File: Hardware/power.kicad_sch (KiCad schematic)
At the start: 52 parts, among them J1 USB4110GFA, Q1 AO3407A, U1 TPS54302, U2 USBLC6-2SC6, U3 INA226, U4 AP63205WU, U5 AP2112K-3.3, U6 AP7343-33W5-7

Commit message: changed hella stuff in firmware plan and hardware pcb layout
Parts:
- removed D2, D3: PMEG3020EH, Diode_SMD:D_SOD-123F, symbol Diode:PMEG3020EH
- removed R6, R7: 0, Resistor_SMD:R_0402_1005Metric, symbol Device:R_Small
- removed R8, R9: 10k, Resistor_SMD:R_0402_1005Metric, symbol Device:R_Small
- C11, C12, C13, R10, R11, R12, U3: now not fitted; now left out of the parts list
- D5: footprint LED_SMD:LED_0402_1005Metric -> LED_SMD:LED_0805_2012Metric
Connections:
- net +5V_REG is gone; now on net +5V: C15.2, C16.2, L2.2, U4.1 (FB)
- net VBAT_Filtered: now also C1.1, C10.2, C2.1, U1.3 (VIN), U4.2 (EN), U4.3 (IN); no longer U3.8 (Vbus)
- net VBAT_MEASURE: no longer C1.1, C10.2, C2.1, U1.3 (VIN), U4.2 (EN), U4.3 (IN)
- net A0: no longer names the net of U3.2 (A0)
- net A1: no longer names the net of U3.1 (A1)
- net I2C2_SCL: no longer names the net of U3.5 (SCL)
- net I2C2_SDA: no longer names the net of U3.4 (SDA)
- net IN+: no longer names the net of C11.1, R10.1, U3.10 (Vin+)
- net IN-: no longer names the net of C11.2, R11.1, U3.9 (Vin-)
- net INA226_ALERT: no longer names the net of U3.3 (~{Alert})
- no-connect marks 4 -> 10

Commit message: hella shit configured, layout progress
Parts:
- C8: footprint Capacitor_SMD:C_0603_1608Metric -> Capacitor_SMD:C_0402_1005Metric
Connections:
- net +5V_USB is gone; now on net +5V: C9.1, J1.A4/B9 (VBUS), J1.B4/A9 (VBUS), U2.5 (VBUS)
- net VBAT renamed +VBAT

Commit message: added zener diode, more layout, Power verificatoin
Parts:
- added D2: BZT52C12-13-F, memo:(zener)SOD-123F_L2.8-W1.8-LS3.7-RD, symbol zener:BZT52C12-13-F
- C18, C20: value 0.1uF -> 1uF
- R3: value 0 -> 100k
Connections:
- net VBAT_Filtered: now also D2.1 (K)
- net at Q1.1 (G), R3.2: now also D2.2 (A)
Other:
- moved on the sheet: R3
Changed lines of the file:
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@@
 	)
 	(junction
-		(at 63.5 76.2)
+		(at 63.5 82.55)
 		(diameter 0)
 		(color 0 0 0 0)
@@
 	)
 	(junction
+		(at 63.5 73.66)
+		(diameter 0)
+		(color 0 0 0 0)
+	)
+	(junction
 		(at 128.27 208.28)
 		(diameter 0)
@@
 	)
 	(junction
-		(at 255.27 55.88)
+		(at 87.63 82.55)
 		(diameter 0)
 		(color 0 0 0 0)
 	)
 	(junction
-		(at 73.66 143.51)
+		(at 255.27 55.88)
 		(diameter 0)
 		(color 0 0 0 0)
 	)
 	(junction
-		(at 87.63 76.2)
+		(at 73.66 143.51)
 		(diameter 0)
 		(color 0 0 0 0)
@@
 	)
 	(junction
+		(at 72.39 59.69)
+		(diameter 0)
+		(color 0 0 0 0)
+	)
+	(junction
 		(at 276.86 222.25)
 		(diameter 0)
@@
 	(wire
 		(pts
+			(xy 87.63 83.82) (xy 87.63 82.55)
+		)
+		(stroke
+			(width 0)
+			(type default)
+		)
+	)
+	(wire
+		(pts
 			(xy 114.3 207.01) (xy 114.3 209.55)
 		)
@@
 	(wire
 		(pts
-			(xy 63.5 67.31) (xy 63.5 68.58)
+			(xy 63.5 67.31) (xy 63.5 73.66)
 		)
 		(stroke
@@
 	(wire
 		(pts
+			(xy 72.39 73.66) (xy 63.5 73.66)
+		)
+		(stroke
+			(width 0)
+			(type default)
+		)
+	)
+	(wire
+		(pts
 			(xy 351.79 90.17) (xy 370.84 90.17)
 		)
@@
 	(wire
 		(pts
-			(xy 68.58 59.69) (xy 80.01 59.69)
+			(xy 68.58 59.69) (xy 72.39 59.69)
 		)
 		(stroke
@@
 	(wire
 		(pts
+			(xy 87.63 71.12) (xy 87.63 77.47)
+		)
+		(stroke
+			(width 0)
+			(type default)
+		)
+	)
+	(wire
+		(pts
 			(xy 232.41 248.92) (xy 232.41 252.73)
 		)
@@
 	(wire
 		(pts
-			(xy 43.18 71.12) (xy 43.18 76.2)
+			(xy 43.18 71.12) (xy 43.18 82.55)
 		)
 		(stroke
@@
 	(wire
 		(pts
+			(xy 72.39 62.23) (xy 72.39 59.69)
+		)
+		(stroke
+			(width 0)
+			(type default)
+		)
+	)
+	(wire
+		(pts
 			(xy 248.92 252.73) (xy 250.19 252.73)
 		)
@@
 	(wire
 		(pts
+			(xy 87.63 77.47) (xy 87.63 82.55)
+		)
+		(stroke
+			(width 0)
+			(type default)
+		)
+	)
+	(wire
+		(pts
 			(xy 246.38 86.36) (xy 246.38 88.9)
 		)
@@
 	(wire
 		(pts
-			(xy 87.63 76.2) (xy 87.63 77.47)
-		)
-		(stroke
-			(width 0)
-			(type default)
-		)
-	)
-	(wire
-		(pts
 			(xy 256.54 88.9) (xy 256.54 86.36)
 		)
@@
 	(wire
 		(pts
-			(xy 63.5 76.2) (xy 87.63 76.2)
+			(xy 63.5 82.55) (xy 87.63 82.55)
 		)
 		(stroke
@@
 	(wire
 		(pts
-			(xy 43.18 76.2) (xy 63.5 76.2)
+			(xy 43.18 82.55) (xy 63.5 82.55)
 		)
 		(stroke
@@
 	(wire
 		(pts
-			(xy 87.63 76.2) (xy 87.63 71.12)
-		)
-		(stroke
-			(width 0)
-			(type default)
-		)
-	)
-	(wire
-		(pts
 			(xy 40.64 119.38) (xy 31.75 119.38)
 		)
@@
 	(wire
 		(pts
-			(xy 87.63 77.47) (xy 87.63 78.74)
-		)
-		(stroke
-			(width 0)
-			(type default)
-		)
-	)
-	(wire
-		(pts
 			(xy 119.38 119.38) (xy 119.38 114.3)
 		)
@@
 	(wire
 		(pts
+			(xy 72.39 73.66) (xy 72.39 72.39)
+		)
+		(stroke
+			(width 0)
+			(type default)
+		)
+	)
+	(wire
+		(pts
 			(xy 243.84 58.42) (xy 240.03 58.42)
 		)
@@
 	(wire
 		(pts
-			(xy 63.5 73.66) (xy 63.5 76.2)
+			(xy 63.5 80.01) (xy 63.5 82.55)
 		)
 		(stroke
@@
 	(wire
 		(pts
+			(xy 63.5 73.66) (xy 63.5 74.93)
+		)
+		(stroke
+			(width 0)
+			(type default)
+		)
+	)
+	(wire
+		(pts
 			(xy 391.16 214.63) (xy 403.86 214.63)
 		)
@@
 	(wire
 		(pts
+			(xy 72.39 59.69) (xy 80.01 59.69)
+		)
+		(stroke
+			(width 0)
+			(type default)
+		)
+	)
+	(wire
+		(pts
 			(xy 114.3 201.93) (xy 114.3 199.39)
 		)
@@
 	)
 	(symbol
+		(lib_id "zener:BZT52C12-13-F")
+		(at 72.39 67.31 270)
+		(unit 1)
+		(exclude_from_sim no)
+		(in_bom yes)
+		(on_board yes)
+		(dnp no)
+		(property "Reference" "D2"
+			(at 68.58 72.136 90)
+			(effects
+				(font
+					(size 0.762 0.762)
+					(thickness 0.0953)
+				)
+				(justify left)
+			)
+		)
+		(property "Value" "BZT52C12-13-F"
+			(at 68.58 74.676 90)
+			(effects
+				(font
+					(size 0.762 0.762)
+					(thickness 0.0953)
+				)
+				(justify left)
+			)
+		)
+		(property "Footprint" "memo:(zener)SOD-123F_L2.8-W1.8-LS3.7-RD"
+			(at 64.77 67.31 0)
+			(effects
+				(font
+					(size 1.27 1.27)
+				)
+				(hide yes)
+			)
+		)
+		(property "Datasheet" "https://lcsc.com/product-detail/Others_Diodes-Incorporated_BZT52C12-13-F_Diodes-Incorporated-BZT52C12-13-F_C177013.html"
+			(at 62.23 67.31 0)
+			(effects
+				(font
+					(size 1.27 1.27)
+				)
+				(hide yes)
+			)
+		)
+		(property "Description" ""
+			(at 72.39 67.31 0)
+			(effects
+				(font
+					(size 1.27 1.27)
+				)
+				(hide yes)
+			)
+		)
+		(property "LCSC Part" "C177013"
+			(at 59.69 67.31 0)
+			(effects
+				(font
+					(size 1.27 1.27)
+				)
+				(hide yes)
+			)
+		)
+		(pin "2"
+		)
+		(pin "1"
+		)
+		(instances
+			(project ""
+				(path "/affbaa1c-796a-43e2-b357-d8056264fe45/4a7cbebd-f698-4bee-b98f-1e10a25991ff"
+					(reference "D2")
+					(unit 1)
+				)
+			)
+		)
+	)
+	(symbol
 		(lib_id "power:PWR_FLAG")
 		(at 281.94 73.66 0)
@@
 	(symbol
 		(lib_id "power:GND")
-		(at 87.63 78.74 0)
+		(at 87.63 83.82 0)
 		(unit 1)
 		(exclude_from_sim no)
@@
 		(fields_autoplaced yes)
 		(property "Reference" "#PWR07"
-			(at 87.63 85.09 0)
+			(at 87.63 90.17 0)
 			(effects
 				(font
@@
 		)
 		(property "Value" "GND"
-			(at 87.63 83.82 0)
+			(at 87.63 88.9 0)
 			(effects
 				(font
@@
 		)
 		(property "Footprint" ""
-			(at 87.63 78.74 0)
+			(at 87.63 83.82 0)
 			(effects
 				(font
@@
 		)
 		(property "Datasheet" ""
-			(at 87.63 78.74 0)
+			(at 87.63 83.82 0)
 			(effects
 				(font
@@
 		)
 		(property "Description" "Power symbol creates a global label with name \"GND\" , ground"
-			(at 87.63 78.74 0)
+			(at 87.63 83.82 0)
 			(effects
 				(font
@@
 			)
 		)
-		(property "Value" "0.1uF"
+		(property "Value" "1uF"
 			(at 398.272 223.012 0)
 			(effects
@@
 	(symbol
 		(lib_id "Device:R_Small")
-		(at 63.5 71.12 180)
+		(at 63.5 77.47 180)
 		(unit 1)
 		(exclude_from_sim no)
@@
 		(dnp no)
 		(property "Reference" "R3"
-			(at 60.706 71.12 90)
+			(at 60.706 77.47 90)
 			(effects
 				(font
@@
 			)
 		)
-		(property "Value" "0"
-			(at 61.976 71.12 90)
+		(property "Value" "100k"
+			(at 61.976 77.47 90)
 			(effects
 				(font
@@
 		)
 		(property "Footprint" "Resistor_SMD:R_0402_1005Metric"
-			(at 63.5 71.12 0)
+			(at 63.5 77.47 0)
 			(effects
 				(font
@@
 		)
 		(property "Datasheet" "~"
-			(at 63.5 71.12 0)
+			(at 63.5 77.47 0)
 			(effects
 				(font
@@
 		)
 		(property "Description" "Resistor, small symbol"
-			(at 63.5 71.12 0)
+			(at 63.5 77.47 0)
 			(effects
 				(font
@@
 		)
 		(property "Link" ""
-			(at 63.5 71.12 90)
+			(at 63.5 77.47 90)
 			(effects
 				(font
@@
 			)
 		)
-		(property "Value" "0.1uF"
+		(property "Value" "1uF"
 			(at 352.552 224.282 0)
 			(effects

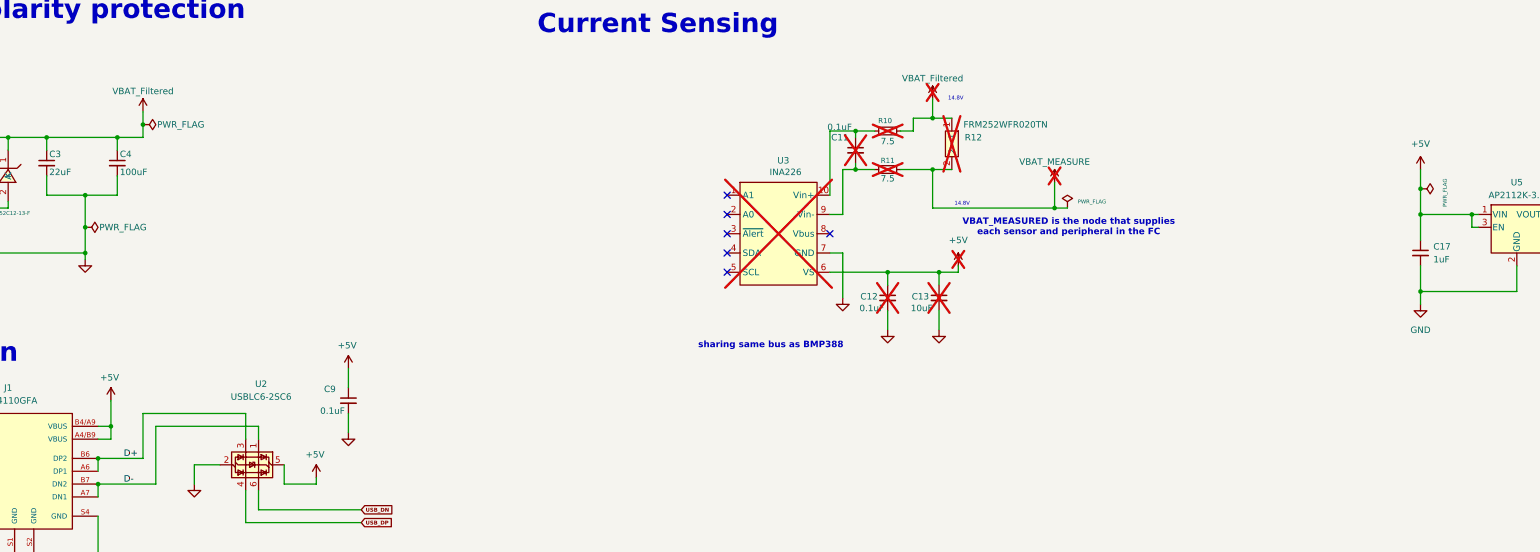
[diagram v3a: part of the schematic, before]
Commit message: fixed 5V rail
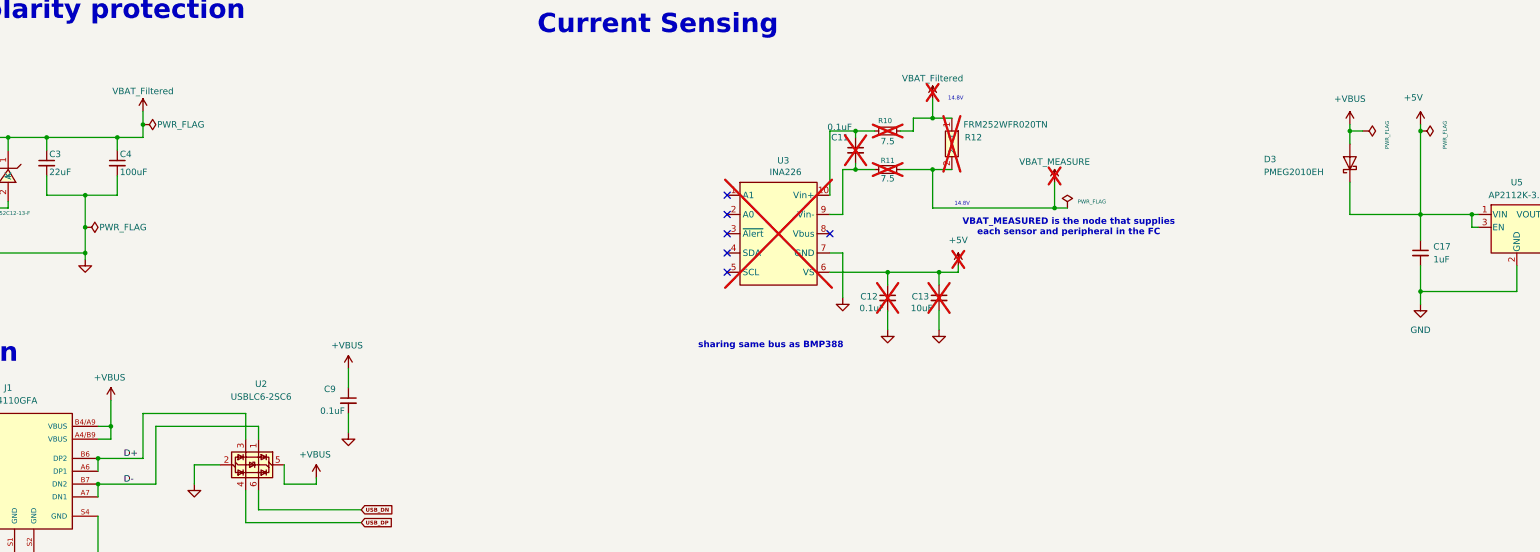
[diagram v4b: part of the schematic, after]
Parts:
- added D3: PMEG2010EH, Diode_SMD:D_SOD-123F, symbol Diode:PMEG2010EH
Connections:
- net +5V: now also D3.1 (K); no longer C9.1, J1.A4/B9 (VBUS), J1.B4/A9 (VBUS), U2.5 (VBUS)
- new net +VBUS: C9.1, D3.2 (A), J1.A4/B9 (VBUS), J1.B4/A9 (VBUS), U2.5 (VBUS)

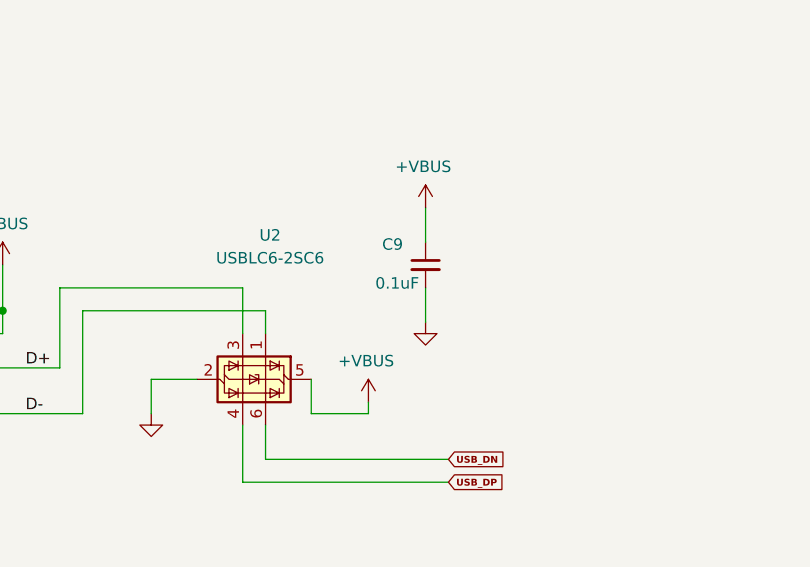
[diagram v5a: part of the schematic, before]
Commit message: fixed the reset schematics
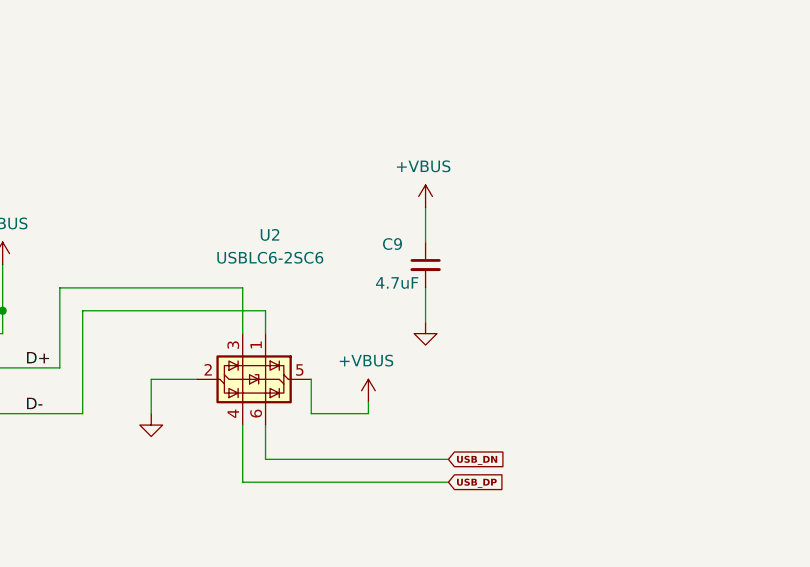
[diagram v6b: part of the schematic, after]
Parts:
- C9: value 0.1uF -> 4.7uF
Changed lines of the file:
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@@
 			)
 		)
-		(property "Value" "0.1uF"
+		(property "Value" "4.7uF"
 			(at 134.112 113.792 0)
 			(effects

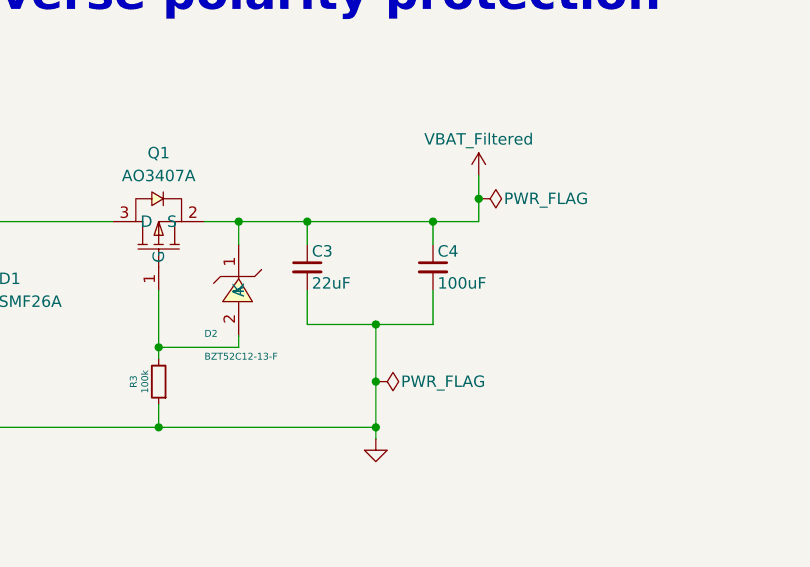
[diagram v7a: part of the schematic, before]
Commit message: corrected vavlues of cap
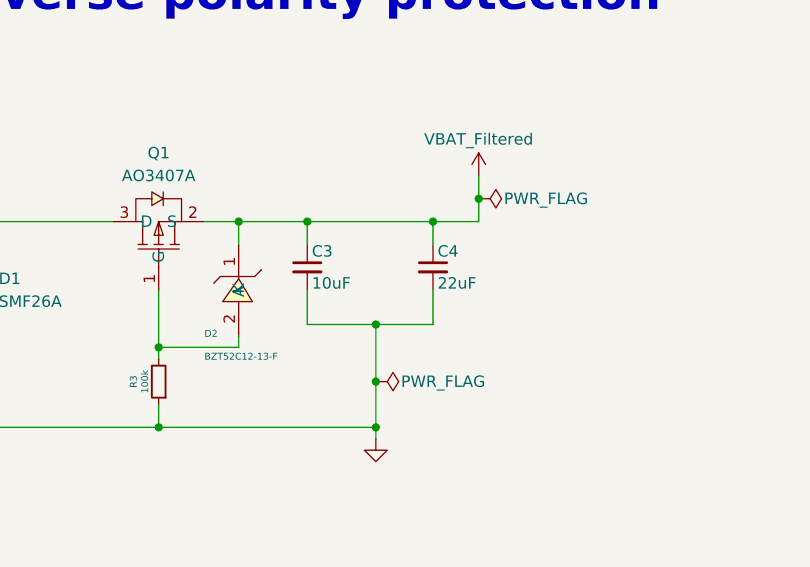
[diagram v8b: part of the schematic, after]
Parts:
- C3: value 22uF -> 10uF
- C4: value 100uF -> 22uF
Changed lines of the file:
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@@
 			)
 		)
-		(property "Value" "22uF"
+		(property "Value" "10uF"
 			(at 80.518 66.548 0)
 			(show_name no)
@@
 			)
 		)
-		(property "Value" "100uF"
+		(property "Value" "22uF"
 			(at 94.488 66.548 0)
 			(show_name no)
